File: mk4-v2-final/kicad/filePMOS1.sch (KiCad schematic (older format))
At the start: 7 parts, among them Q6 Q_PMOS_GDS, Q8 2N3904

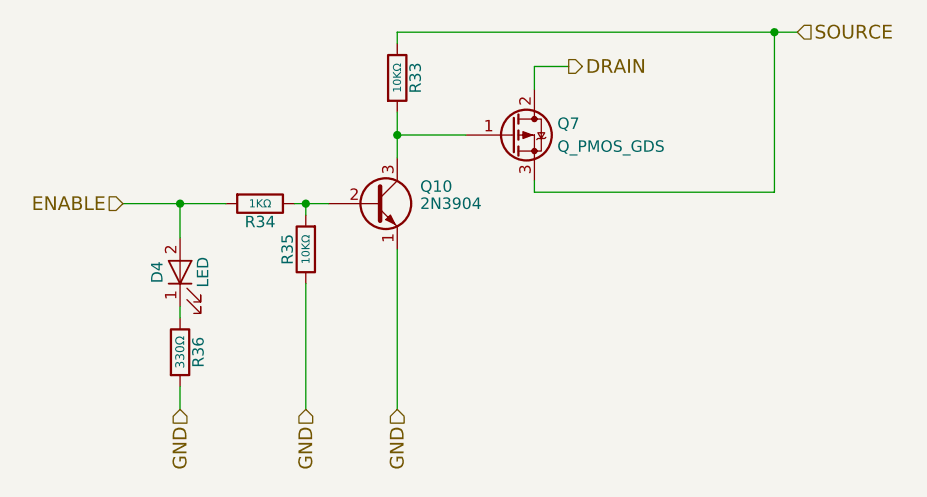
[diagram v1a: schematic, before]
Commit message: added headnight diodes, I don't think software control of them is going to be possible
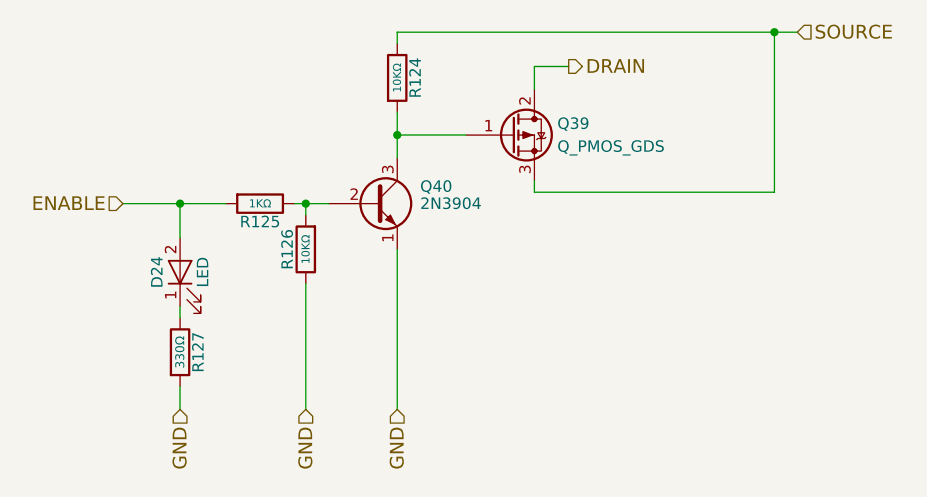
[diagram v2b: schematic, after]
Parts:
- renumbered D3 to D4, Q6 to Q3, Q8 to Q4, R29 to R27, R30 to R28, R31 to R29, R32 to R30

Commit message: schematic is done, footprint association and netlist are also done
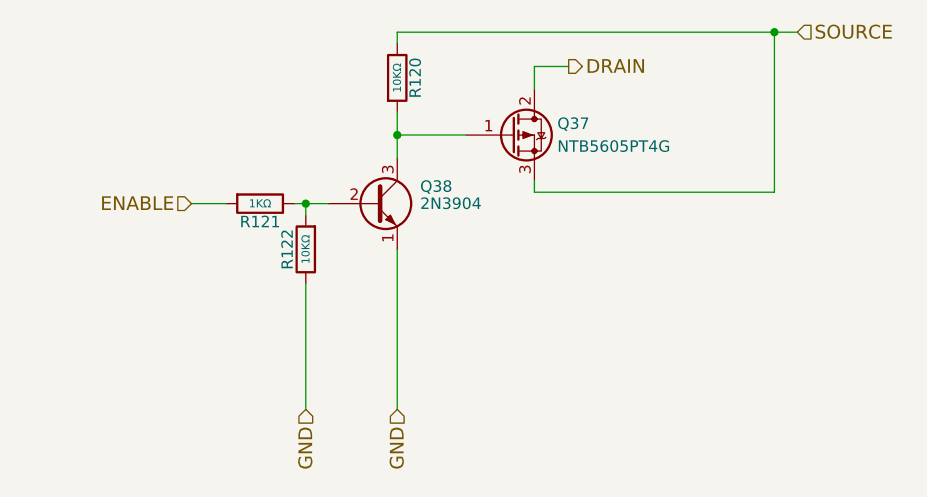
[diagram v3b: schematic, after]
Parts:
- removed D4: LED, LEDs:LED_D5.0mm, symbol LED
- removed R30: 330Ω, Resistors_THT:R_Axial_DIN0207_L6.3mm_D2.5mm_P10.16mm_Horizontal, symbol R
- Q3: value Q_PMOS_GDS -> NTB5605PT4G; footprint TO_SOT_Packages_THT:TO-220-3_Vertical -> TO_SOT_Packages_SMD:TO-263-3_TabPin2; digikey-pn (none) -> NTB5605PT4GOSCT-ND; mfg-pn (none) -> NTB5605PT4G
- Q4: footprint TO_SOT_Packages_THT:TO-92_Molded_Narrow -> TO_SOT_Packages_THT:TO-92_Inline_Wide; digikey-pn (none) -> 2N3904FS-ND; mfg-pn (none) -> 2N3904BU
- R27, R29: footprint Resistors_THT:R_Axial_DIN0207_L6.3mm_D2.5mm_P10.16mm_Horizontal -> Resistors_THT:R_Axial_DIN0204_L3.6mm_D1.6mm_P5.08mm_Horizontal; digikey-pn (none) -> BC10.0KXCT-ND; mfg-pn (none) -> MBA02040C1002FRP00
- R28: footprint Resistors_THT:R_Axial_DIN0207_L6.3mm_D2.5mm_P10.16mm_Horizontal -> Resistors_THT:R_Axial_DIN0204_L3.6mm_D1.6mm_P5.08mm_Horizontal; digikey-pn (none) -> BC1.00KXCT-ND; mfg-pn (none) -> MBA02040C1001FRP00
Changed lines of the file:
@@
 EESchema Schematic File Version 2
-LIBS:hitchco-mk4-rescue
 LIBS:power
 LIBS:device
@@
 LIBS:cd4013b
 LIBS:ncs3s1205sc
+LIBS:lca715
+LIBS:SN74HC595N
+LIBS:CD74HC4067
 LIBS:hitchco-mk4-cache
 EELAYER 25 0
@@
 $Descr USLetter 11000 8500
 encoding utf-8
-Sheet 15 54
+Sheet 51 54
 Title ""
 Date ""
@@
 AR Path="/59DEA30F/5B193940/59E17AAC" Ref="Q38"  Part="1"
 AR Path="/59DEA30F/5B1AFE32/59E17AAC" Ref="Q40"  Part="1"
-F 0 "Q40" H 4850 4875 50  0000 L CNN
+F 0 "Q38" H 4850 4875 50  0000 L CNN
 F 1 "2N3904" H 4850 4800 50  0000 L CNN
-F 2 "TO_SOT_Packages_THT:TO-92_Molded_Narrow" H 4850 4725 50  0001 L CIN
-F 3 "" H 4650 4800 50  0001 L CNN
+F 2 "TO_SOT_Packages_THT:TO-92_Inline_Wide" H 4850 4725 50  0001 L CIN
+F 3 "https://www.fairchildsemi.com/datasheets/MM/MMBT3904.pdf" H 4650 4800 50  0001 L CNN
+F 4 "2N3904FS-ND" H 4650 4800 60  0001 C CNN "digikey-pn"
+F 5 "2N3904BU" H 4650 4800 60  0001 C CNN "mfg-pn"
 	1    4650 4800
 	1    0    0    -1
@@
 AR Path="/59DEA30F/5B193940/59E17AB3" Ref="R121"  Part="1"
 AR Path="/59DEA30F/5B1AFE32/59E17AB3" Ref="R125"  Part="1"
-F 0 "R125" V 4230 4800 50  0000 C CNN
+F 0 "R121" V 4230 4800 50  0000 C CNN
 F 1 "1KΩ" V 4150 4800 35  0000 C CNN
-F 2 "Resistors_THT:R_Axial_DIN0207_L6.3mm_D2.5mm_P10.16mm_Horizontal" V 4080 4800 50  0001 C CNN
+F 2 "Resistors_THT:R_Axial_DIN0204_L3.6mm_D1.6mm_P5.08mm_Horizontal" V 4080 4800 50  0001 C CNN
 F 3 "" H 4150 4800 50  0001 C CNN
+F 4 "BC1.00KXCT-ND" H 4230 4900 50  0001 C CNN "digikey-pn"
+F 5 "MBA02040C1001FRP00" H 4230 4900 50  0001 C CNN "mfg-pn"
 	1    4150 4800
 	0    1    1    0
 $EndComp
-Text HLabel 5500 4200 2    60   Output ~ 0
-DRAIN
 $Comp
 L R R27
@@
 AR Path="/59DEA30F/5B193940/59E17ABB" Ref="R120"  Part="1"
 AR Path="/59DEA30F/5B1AFE32/59E17ABB" Ref="R124"  Part="1"
-F 0 "R124" V 4830 4250 50  0000 C CNN
+F 0 "R120" V 4830 4250 50  0000 C CNN
 F 1 "10KΩ" V 4750 4250 35  0000 C CNN
-F 2 "Resistors_THT:R_Axial_DIN0207_L6.3mm_D2.5mm_P10.16mm_Horizontal" V 4680 4250 50  0001 C CNN
+F 2 "Resistors_THT:R_Axial_DIN0204_L3.6mm_D1.6mm_P5.08mm_Horizontal" V 4680 4250 50  0001 C CNN
 F 3 "" H 4750 4250 50  0001 C CNN
+F 4 "BC10.0KXCT-ND" H 4830 4350 50  0001 C CNN "digikey-pn"
+F 5 "MBA02040C1002FRP00" H 4830 4350 50  0001 C CNN "mfg-pn"
 	1    4750 4250
 	1    0    0    -1
@@
 AR Path="/59DEA30F/5B193940/59E17AC2" Ref="R122"  Part="1"
 AR Path="/59DEA30F/5B1AFE32/59E17AC2" Ref="R126"  Part="1"
-F 0 "R126" V 4430 5000 50  0000 C CNN
+F 0 "R122" V 4430 5000 50  0000 C CNN
 F 1 "10KΩ" V 4350 5000 35  0000 C CNN
-F 2 "Resistors_THT:R_Axial_DIN0207_L6.3mm_D2.5mm_P10.16mm_Horizontal" V 4280 5000 50  0001 C CNN
+F 2 "Resistors_THT:R_Axial_DIN0204_L3.6mm_D1.6mm_P5.08mm_Horizontal" V 4280 5000 50  0001 C CNN
 F 3 "" H 4350 5000 50  0001 C CNN
+F 4 "BC10.0KXCT-ND" H 4430 5100 50  0001 C CNN "digikey-pn"
+F 5 "MBA02040C1002FRP00" H 4430 5100 50  0001 C CNN "mfg-pn"
 	1    4350 5000
 	-1   0    0    1
 $EndComp
-Text HLabel 3550 4800 0    60   Input ~ 0
-ENABLE
-Wire Wire Line
-	4750 5000 4750 5700
-Connection ~ 4750 4500
-Wire Wire Line
-	5500 4200 5350 4200
-Wire Wire Line
-	5350 4200 5350 4300
-Wire Wire Line
-	4300 4800 4450 4800
-Connection ~ 4350 4800
-Wire Wire Line
-	4350 5150 4350 5700
-Wire Wire Line
-	4350 4800 4350 4850
-Wire Wire Line
-	3550 4800 4000 4800
-Wire Wire Line
-	4750 4400 4750 4600
-Wire Wire Line
-	5050 4500 4750 4500
-Wire Wire Line
-	4750 4050 6500 4050
-Wire Wire Line
-	4750 4050 4750 4100
-Connection ~ 6400 4050
-Wire Wire Line
-	6400 4750 5350 4750
-Wire Wire Line
-	5350 4750 5350 4700
-Text HLabel 6500 4050 2    60   Input ~ 0
-SOURCE
-Text HLabel 4350 5700 3    60   Input ~ 0
-GND
-Text HLabel 4750 5700 3    60   Input ~ 0
-GND
-Wire Wire Line
-	6400 4050 6400 4750
-Text HLabel 3800 5700 3    60   Input ~ 0
-GND
-Wire Wire Line
-	3800 4800 3800 4950
-Connection ~ 3800 4800
-$Comp
-L R R30
-U 1 1 5A60FA4A
-P 3800 5450
-AR Path="/59DEA30F/5A0AB280/5A60FA4A" Ref="R30"  Part="1"
-AR Path="/59DEA30F/5A0AB292/5A60FA4A" Ref="R34"  Part="1"
-AR Path="/59DEA30F/5A0DDF97/5A60FA4A" Ref="R41"  Part="1"
-AR Path="/59DEA30F/5A0E0621/5A60FA4A" Ref="R45"  Part="1"
-AR Path="/59DEA30F/5A5CD337/5A60FA4A" Ref="R68"  Part="1"
-AR Path="/59DEA30F/5A5D22C5/5A60FA4A" Ref="R72"  Part="1"
-AR Path="/59DEA30F/5A5D4870/5A60FA4A" Ref="R76"  Part="1"
-AR Path="/59DEA30F/5B102666/5A60FA4A" Ref="R93"  Part="1"
-AR Path="/59DEA30F/5B108B04/5A60FA4A" Ref="R97"  Part="1"
-AR Path="/59DEA30F/5B11D41F/5A60FA4A" Ref="R101"  Part="1"
-AR Path="/59DEA30F/5B162D7A/5A60FA4A" Ref="R105"  Part="1"
-AR Path="/59DEA30F/5B18C9DE/5A60FA4A" Ref="R113"  Part="1"
-AR Path="/59DEA30F/5B18D901/5A60FA4A" Ref="R117"  Part="1"
-AR Path="/59DEA30F/5B193940/5A60FA4A" Ref="R123"  Part="1"
-AR Path="/59DEA30F/5B1AFE32/5A60FA4A" Ref="R127"  Part="1"
-F 0 "R127" V 3880 5450 50  0000 C CNN
-F 1 "330Ω" V 3800 5450 39  0000 C CNN
-F 2 "Resistors_THT:R_Axial_DIN0207_L6.3mm_D2.5mm_P10.16mm_Horizontal" V 3730 5450 50  0001 C CNN
-F 3 "" H 3800 5450 50  0001 C CNN
-	1    3800 5450
-	1    0    0    -1
-$EndComp
-Wire Wire Line
-	3800 5600 3800 5700
-$Comp
-L LED D4
-U 1 1 5A23876F
-P 3800 5100
-AR Path="/59DEA30F/5A0AB280/5A23876F" Ref="D4"  Part="1"
-AR Path="/59DEA30F/5A0AB292/5A23876F" Ref="D5"  Part="1"
-AR Path="/59DEA30F/5A0DDF97/5A23876F" Ref="D7"  Part="1"
-AR Path="/59DEA30F/5A0E0621/5A23876F" Ref="D8"  Part="1"
-AR Path="/59DEA30F/5A5CD337/5A23876F" Ref="D11"  Part="1"
-AR Path="/59DEA30F/5A5D22C5/5A23876F" Ref="D12"  Part="1"
-AR Path="/59DEA30F/5A5D4870/5A23876F" Ref="D13"  Part="1"
-AR Path="/59DEA30F/5B102666/5A23876F" Ref="D15"  Part="1"
-AR Path="/59DEA30F/5B108B04/5A23876F" Ref="D16"  Part="1"
-AR Path="/59DEA30F/5B11D41F/5A23876F" Ref="D17"  Part="1"
-AR Path="/59DEA30F/5B162D7A/5A23876F" Ref="D18"  Part="1"
-AR Path="/59DEA30F/5B18C9DE/5A23876F" Ref="D21"  Part="1"
-AR Path="/59DEA30F/5B18D901/5A23876F" Ref="D22"  Part="1"
-AR Path="/59DEA30F/5B193940/5A23876F" Ref="D23"  Part="1"
-AR Path="/59DEA30F/5B1AFE32/5A23876F" Ref="D24"  Part="1"
-F 0 "D24" H 3800 5200 50  0000 C CNN
-F 1 "LED" H 3800 5000 50  0000 C CNN
-F 2 "LEDs:LED_D5.0mm" H 3800 5100 50  0001 C CNN
-F 3 "http://www.kingbrightusa.com/images/catalog/SPEC/WP7113ID.pdf" H 3800 5100 50  0001 C CNN
-	1    3800 5100
-	0    -1   -1   0
-$EndComp
-Wire Wire Line
-	3800 5250 3800 5300
 $Comp
 L Q_PMOS_GDS Q3
@@
 AR Path="/59DEA30F/5B193940/5A2F44DB" Ref="Q37"  Part="1"
 AR Path="/59DEA30F/5B1AFE32/5A2F44DB" Ref="Q39"  Part="1"
-F 0 "Q39" H 5450 4550 50  0000 L CNN
-F 1 "Q_PMOS_GDS" H 5450 4450 50  0000 L CNN
-F 2 "TO_SOT_Packages_THT:TO-220-3_Vertical" H 5450 4600 50  0001 C CNN
-F 3 "" H 5250 4500 50  0001 C CNN
+F 0 "Q37" H 5450 4550 50  0000 L CNN
+F 1 "NTB5605PT4G" H 5450 4450 50  0000 L CNN
+F 2 "TO_SOT_Packages_SMD:TO-263-3_TabPin2" H 5450 4600 50  0001 C CNN
+F 3 "http://www.onsemi.com/pub/Collateral/NTB5605P-D.PDF" H 5250 4500 50  0001 C CNN
+F 4 "NTB5605PT4GOSCT-ND" H 5250 4500 60  0001 C CNN "digikey-pn"
+F 5 "NTB5605PT4G" H 5250 4500 60  0001 C CNN "mfg-pn"
 	1    5250 4500
 	1    0    0    -1
 $EndComp
+Text HLabel 5500 4200 2    60   Output ~ 0
+DRAIN
+Text HLabel 3850 4800 0    60   Input ~ 0
+ENABLE
+Text HLabel 6500 4050 2    60   Input ~ 0
+SOURCE
+Text HLabel 4350 5700 3    60   Input ~ 0
+GND
+Text HLabel 4750 5700 3    60   Input ~ 0
+GND
+Wire Wire Line
+	4750 5000 4750 5700
+Wire Wire Line
+	5500 4200 5350 4200
+Wire Wire Line
+	5350 4200 5350 4300
+Wire Wire Line
+	4300 4800 4450 4800
+Wire Wire Line
+	4350 5150 4350 5700
+Wire Wire Line
+	4350 4800 4350 4850
+Wire Wire Line
+	4750 4400 4750 4600
+Wire Wire Line
+	5050 4500 4750 4500
+Wire Wire Line
+	4750 4050 6500 4050
+Wire Wire Line
+	4750 4050 4750 4100
+Wire Wire Line
+	6400 4750 5350 4750
+Wire Wire Line
+	5350 4750 5350 4700
+Wire Wire Line
+	6400 4050 6400 4750
+Wire Wire Line
+	3850 4800 4000 4800
+Connection ~ 4750 4500
+Connection ~ 4350 4800
+Connection ~ 6400 4050
 $EndSCHEMATC

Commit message: all components on the board
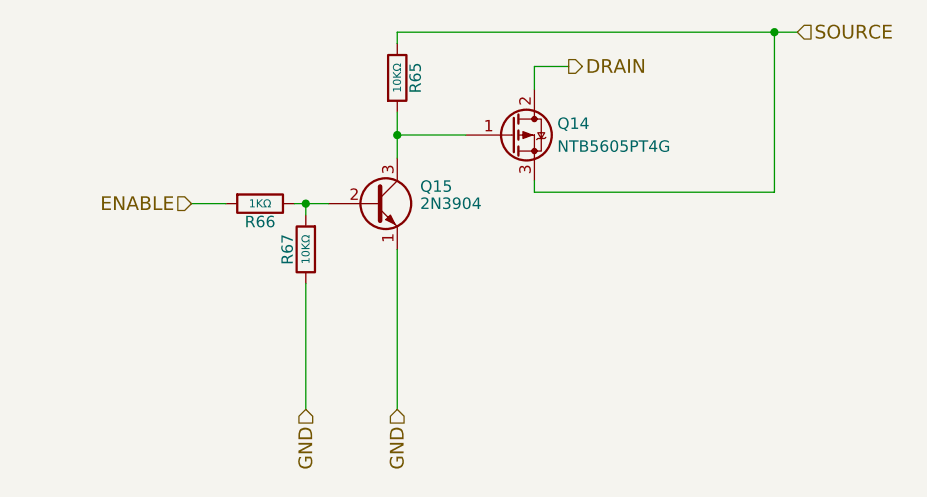
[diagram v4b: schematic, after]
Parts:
- Q4: footprint TO_SOT_Packages_THT:TO-92_Inline_Wide -> TO_SOT_Packages_THT:TO-92_Inline_Narrow_Oval
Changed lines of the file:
@@
 $Descr USLetter 11000 8500
 encoding utf-8
-Sheet 51 54
+Sheet 12 54
 Title ""
 Date ""
@@
 AR Path="/59DEA30F/5B193940/59E17AAC" Ref="Q38"  Part="1"
 AR Path="/59DEA30F/5B1AFE32/59E17AAC" Ref="Q40"  Part="1"
-F 0 "Q38" H 4850 4875 50  0000 L CNN
+F 0 "Q15" H 4850 4875 50  0000 L CNN
 F 1 "2N3904" H 4850 4800 50  0000 L CNN
-F 2 "TO_SOT_Packages_THT:TO-92_Inline_Wide" H 4850 4725 50  0001 L CIN
+F 2 "TO_SOT_Packages_THT:TO-92_Inline_Narrow_Oval" H 4850 4725 50  0001 L CIN
 F 3 "https://www.fairchildsemi.com/datasheets/MM/MMBT3904.pdf" H 4650 4800 50  0001 L CNN
 F 4 "2N3904FS-ND" H 4650 4800 60  0001 C CNN "digikey-pn"
@@
 AR Path="/59DEA30F/5B193940/59E17AB3" Ref="R121"  Part="1"
 AR Path="/59DEA30F/5B1AFE32/59E17AB3" Ref="R125"  Part="1"
-F 0 "R121" V 4230 4800 50  0000 C CNN
+F 0 "R66" V 4230 4800 50  0000 C CNN
 F 1 "1KΩ" V 4150 4800 35  0000 C CNN
 F 2 "Resistors_THT:R_Axial_DIN0204_L3.6mm_D1.6mm_P5.08mm_Horizontal" V 4080 4800 50  0001 C CNN
@@
 AR Path="/59DEA30F/5B193940/59E17ABB" Ref="R120"  Part="1"
 AR Path="/59DEA30F/5B1AFE32/59E17ABB" Ref="R124"  Part="1"
-F 0 "R120" V 4830 4250 50  0000 C CNN
+F 0 "R65" V 4830 4250 50  0000 C CNN
 F 1 "10KΩ" V 4750 4250 35  0000 C CNN
 F 2 "Resistors_THT:R_Axial_DIN0204_L3.6mm_D1.6mm_P5.08mm_Horizontal" V 4680 4250 50  0001 C CNN
@@
 AR Path="/59DEA30F/5B193940/59E17AC2" Ref="R122"  Part="1"
 AR Path="/59DEA30F/5B1AFE32/59E17AC2" Ref="R126"  Part="1"
-F 0 "R122" V 4430 5000 50  0000 C CNN
+F 0 "R67" V 4430 5000 50  0000 C CNN
 F 1 "10KΩ" V 4350 5000 35  0000 C CNN
 F 2 "Resistors_THT:R_Axial_DIN0204_L3.6mm_D1.6mm_P5.08mm_Horizontal" V 4280 5000 50  0001 C CNN
@@
 AR Path="/59DEA30F/5B193940/5A2F44DB" Ref="Q37"  Part="1"
 AR Path="/59DEA30F/5B1AFE32/5A2F44DB" Ref="Q39"  Part="1"
-F 0 "Q37" H 5450 4550 50  0000 L CNN
+F 0 "Q14" H 5450 4550 50  0000 L CNN
 F 1 "NTB5605PT4G" H 5450 4450 50  0000 L CNN
 F 2 "TO_SOT_Packages_SMD:TO-263-3_TabPin2" H 5450 4600 50  0001 C CNN
